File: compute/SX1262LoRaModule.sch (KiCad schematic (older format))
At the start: 28 parts, among them U201 SX1262, U202 PE4259, Y201 TBD

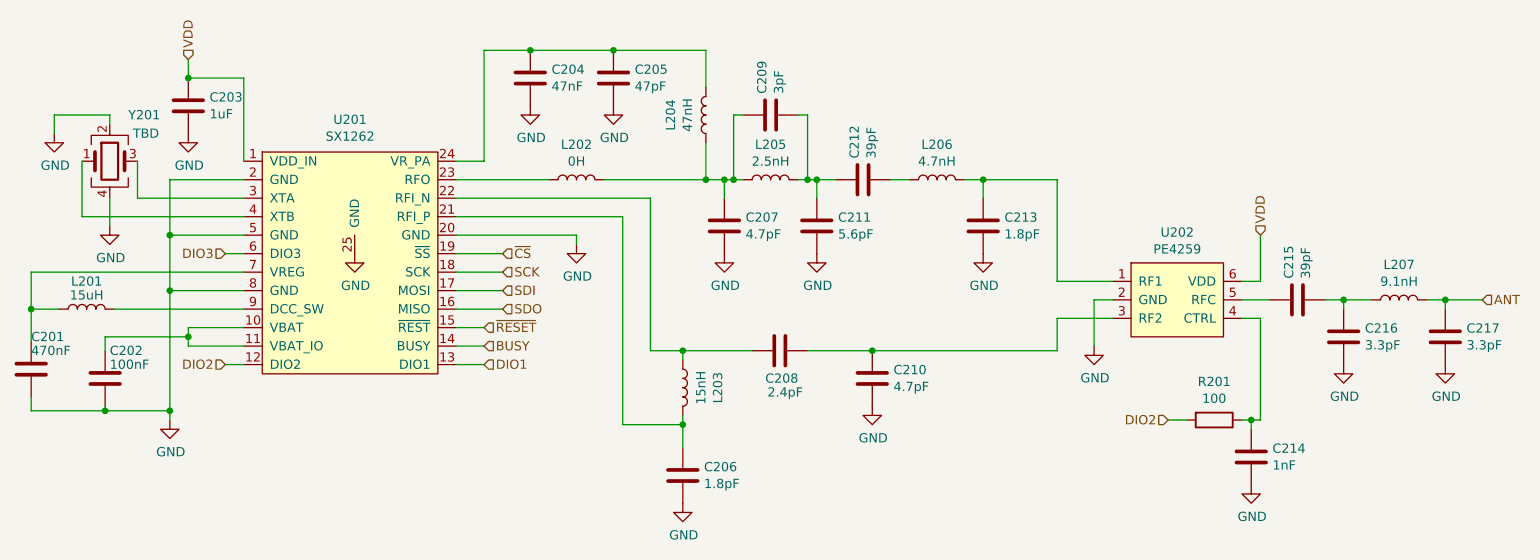
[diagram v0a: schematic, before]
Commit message: Adding more GND testpoints
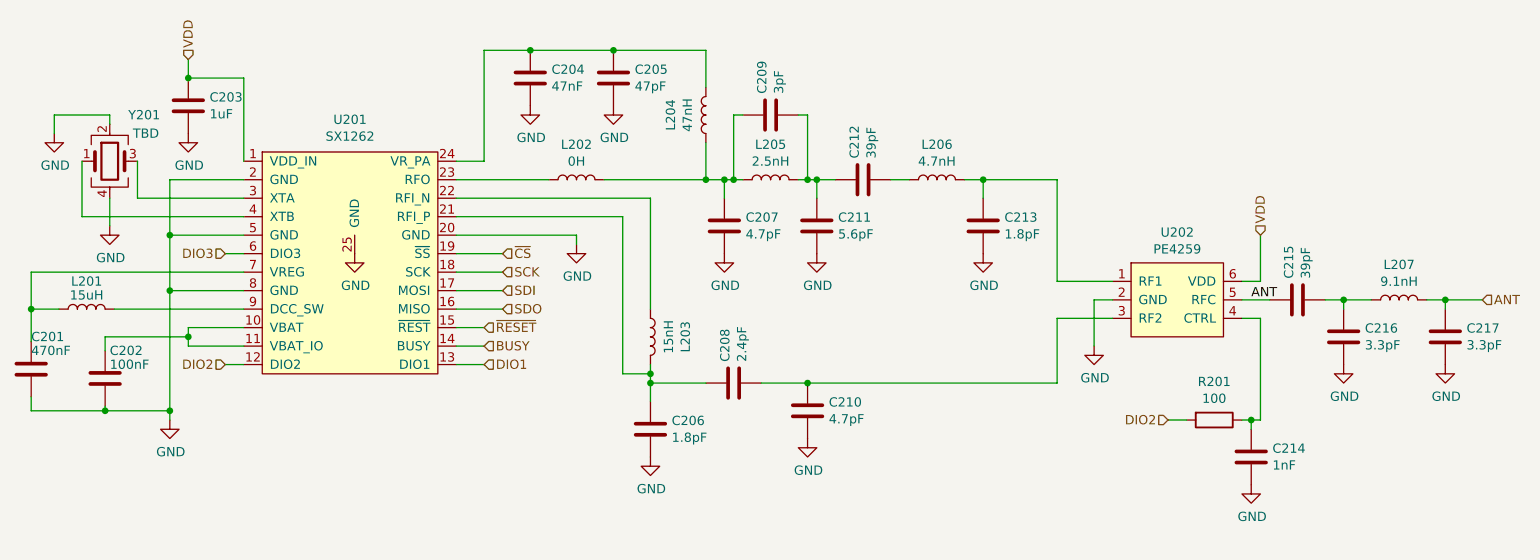
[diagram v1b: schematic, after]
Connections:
- net ANT: now also C215.1, U202.5 (RFC)
- net at L203.1, U201.22 (RFI_N): no longer C208.1
- net at C206.1, L203.2, U201.21 (RFI_P): now also C208.1
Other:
- moved on the sheet: C206, C208, C210, L203
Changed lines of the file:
@@
 L Device:L L203
 U 1 1 618C8BAD
-P 6025 4425
+P 5850 4150
 AR Path="/624C3AFD/618C8BAD" Ref="L203"  Part="1"
 AR Path="/61FFC2A4/618C8BAD" Ref="L?"  Part="1"
-F 0 "L203" V 6215 4425 50  0000 C CNN
-F 1 "15nH" V 6124 4425 50  0000 C CNN
-F 2 "Inductor_SMD:L_0402_1005Metric_Pad0.77x0.64mm_HandSolder" H 6025 4425 50  0001 C CNN
-F 3 "~" H 6025 4425 50  0001 C CNN
-F 4 "" V 6025 4425 50  0001 C CNN "MFN"
-F 5 "" V 6025 4425 50  0001 C CNN "MFP"
-F 6 "" V 6025 4425 50  0001 C CNN "S1PN"
-F 7 "" V 6025 4425 50  0001 C CNN "S1PL"
-F 8 "DNL" V 6025 4425 50  0001 C CNN "Notes"
-	1    6025 4425
+F 0 "L203" V 6040 4150 50  0000 C CNN
+F 1 "15nH" V 5949 4150 50  0000 C CNN
+F 2 "Inductor_SMD:L_0402_1005Metric_Pad0.77x0.64mm_HandSolder" H 5850 4150 50  0001 C CNN
+F 3 "~" H 5850 4150 50  0001 C CNN
+F 4 "" V 5850 4150 50  0001 C CNN "MFN"
+F 5 "" V 5850 4150 50  0001 C CNN "MFP"
+F 6 "" V 5850 4150 50  0001 C CNN "S1PN"
+F 7 "" V 5850 4150 50  0001 C CNN "S1PL"
+F 8 "DNL" V 5850 4150 50  0001 C CNN "Notes"
+	1    5850 4150
 	1    0    0    -1
 $EndComp
 Wire Wire Line
 	4800 3400 5850 3400
+Wire Wire Line
+	5850 3400 5850 4000
 Wire Wire Line
 	4800 3500 5700 3500
@@
 L Device:C C206
 U 1 1 618CE91A
-P 6025 4900
+P 5850 4650
 AR Path="/624C3AFD/618CE91A" Ref="C206"  Part="1"
 AR Path="/61FFC2A4/618CE91A" Ref="C?"  Part="1"
-F 0 "C206" H 6140 4946 50  0000 L CNN
-F 1 "1.8pF" H 6140 4855 50  0000 L CNN
-F 2 "Capacitor_SMD:C_0402_1005Metric_Pad0.74x0.62mm_HandSolder" H 6063 4750 50  0001 C CNN
-F 3 "~" H 6025 4900 50  0001 C CNN
-F 4 "" H 6025 4900 50  0001 C CNN "MFN"
-F 5 "" H 6025 4900 50  0001 C CNN "MFP"
-F 6 "" H 6025 4900 50  0001 C CNN "S1PN"
-F 7 "" H 6025 4900 50  0001 C CNN "S1PL"
-F 8 "DNL" H 6025 4900 50  0001 C CNN "Notes"
-	1    6025 4900
-	1    0    0    -1
-$EndComp
+F 0 "C206" H 5965 4696 50  0000 L CNN
+F 1 "1.8pF" H 5965 4605 50  0000 L CNN
+F 2 "Capacitor_SMD:C_0402_1005Metric_Pad0.74x0.62mm_HandSolder" H 5888 4500 50  0001 C CNN
+F 3 "~" H 5850 4650 50  0001 C CNN
+F 4 "" H 5850 4650 50  0001 C CNN "MFN"
+F 5 "" H 5850 4650 50  0001 C CNN "MFP"
+F 6 "" H 5850 4650 50  0001 C CNN "S1PN"
+F 7 "" H 5850 4650 50  0001 C CNN "S1PL"
+F 8 "DNL" H 5850 4650 50  0001 C CNN "Notes"
+	1    5850 4650
+	1    0    0    -1
+$EndComp
+Wire Wire Line
+	5850 4300 5850 4350
+Wire Wire Line
+	5700 4350 5850 4350
+Wire Wire Line
+	5700 3500 5700 4350
+Connection ~ 5850 4350
 $Comp
 L power:GND #PWR0209
 U 1 1 618D373E
-P 6025 5050
+P 5850 4800
 AR Path="/624C3AFD/618D373E" Ref="#PWR0209"  Part="1"
 AR Path="/61FFC2A4/618D373E" Ref="#PWR?"  Part="1"
-F 0 "#PWR0209" H 6025 4800 50  0001 C CNN
-F 1 "GND" H 6030 4877 50  0000 C CNN
-F 2 "" H 6025 5050 50  0001 C CNN
-F 3 "" H 6025 5050 50  0001 C CNN
-	1    6025 5050
+F 0 "#PWR0209" H 5850 4550 50  0001 C CNN
+F 1 "GND" H 5855 4627 50  0000 C CNN
+F 2 "" H 5850 4800 50  0001 C CNN
+F 3 "" H 5850 4800 50  0001 C CNN
+	1    5850 4800
 	1    0    0    -1
 $EndComp
@@
 L Device:C C208
 U 1 1 618D3CBD
-P 6550 4225
+P 6300 4400
 AR Path="/624C3AFD/618D3CBD" Ref="C208"  Part="1"
 AR Path="/61FFC2A4/618D3CBD" Ref="C?"  Part="1"
-F 0 "C208" V 6400 4125 50  0000 L CNN
-F 1 "2.4pF" V 6325 4100 50  0000 L CNN
-F 2 "Capacitor_SMD:C_0402_1005Metric_Pad0.74x0.62mm_HandSolder" H 6588 4075 50  0001 C CNN
-F 3 "~" H 6550 4225 50  0001 C CNN
-F 4 "" H 6550 4225 50  0001 C CNN "MFN"
-F 5 "" H 6550 4225 50  0001 C CNN "MFP"
-F 6 "Digikey" H 6550 4225 50  0001 C CNN "S1PN"
-F 7 "https://www.digikey.com/en/products/detail/taiyo-yuden/EVK105CH0R3BW-F/1169601" H 6550 4225 50  0001 C CNN "S1PL"
-F 8 "DNL" H 6550 4225 50  0001 C CNN "Notes"
-	1    6550 4225
+F 0 "C208" H 6415 4446 50  0000 L CNN
+F 1 "2.4pF" H 6415 4355 50  0000 L CNN
+F 2 "Capacitor_SMD:C_0402_1005Metric_Pad0.74x0.62mm_HandSolder" H 6338 4250 50  0001 C CNN
+F 3 "~" H 6300 4400 50  0001 C CNN
+F 4 "" H 6300 4400 50  0001 C CNN "MFN"
+F 5 "" H 6300 4400 50  0001 C CNN "MFP"
+F 6 "Digikey" H 6300 4400 50  0001 C CNN "S1PN"
+F 7 "https://www.digikey.com/en/products/detail/taiyo-yuden/EVK105CH0R3BW-F/1169601" H 6300 4400 50  0001 C CNN "S1PL"
+F 8 "DNL" H 6300 4400 50  0001 C CNN "Notes"
+	1    6300 4400
 	0    -1   -1   0
 $EndComp
@@
 L Device:C C210
 U 1 1 618D4647
-P 7050 4375
+P 6700 4550
 AR Path="/624C3AFD/618D4647" Ref="C210"  Part="1"
 AR Path="/61FFC2A4/618D4647" Ref="C?"  Part="1"
-F 0 "C210" H 7165 4421 50  0000 L CNN
-F 1 "4.7pF" H 7165 4330 50  0000 L CNN
-F 2 "Capacitor_SMD:C_0402_1005Metric_Pad0.74x0.62mm_HandSolder" H 7088 4225 50  0001 C CNN
-F 3 "~" H 7050 4375 50  0001 C CNN
-F 4 "" H 7050 4375 50  0001 C CNN "MFN"
-F 5 "" H 7050 4375 50  0001 C CNN "MFP"
-F 6 "" H 7050 4375 50  0001 C CNN "S1PN"
-F 7 "" H 7050 4375 50  0001 C CNN "S1PL"
-F 8 "DNL" H 7050 4375 50  0001 C CNN "Notes"
-	1    7050 4375
-	1    0    0    -1
-$EndComp
+F 0 "C210" H 6815 4596 50  0000 L CNN
+F 1 "4.7pF" H 6815 4505 50  0000 L CNN
+F 2 "Capacitor_SMD:C_0402_1005Metric_Pad0.74x0.62mm_HandSolder" H 6738 4400 50  0001 C CNN
+F 3 "~" H 6700 4550 50  0001 C CNN
+F 4 "" H 6700 4550 50  0001 C CNN "MFN"
+F 5 "" H 6700 4550 50  0001 C CNN "MFP"
+F 6 "" H 6700 4550 50  0001 C CNN "S1PN"
+F 7 "" H 6700 4550 50  0001 C CNN "S1PL"
+F 8 "DNL" H 6700 4550 50  0001 C CNN "Notes"
+	1    6700 4550
+	1    0    0    -1
+$EndComp
+Wire Wire Line
+	5850 4350 5850 4400
+Wire Wire Line
+	5850 4400 6150 4400
+Connection ~ 5850 4400
+Wire Wire Line
+	5850 4400 5850 4500
+Wire Wire Line
+	6450 4400 6700 4400
 $Comp
 L power:GND #PWR0211
 U 1 1 618DD2D6
-P 7050 4525
+P 6700 4700
 AR Path="/624C3AFD/618DD2D6" Ref="#PWR0211"  Part="1"
 AR Path="/61FFC2A4/618DD2D6" Ref="#PWR?"  Part="1"
-F 0 "#PWR0211" H 7050 4275 50  0001 C CNN
-F 1 "GND" H 7055 4352 50  0000 C CNN
-F 2 "" H 7050 4525 50  0001 C CNN
-F 3 "" H 7050 4525 50  0001 C CNN
-	1    7050 4525
-	1    0    0    -1
-$EndComp
+F 0 "#PWR0211" H 6700 4450 50  0001 C CNN
+F 1 "GND" H 6705 4527 50  0000 C CNN
+F 2 "" H 6700 4700 50  0001 C CNN
+F 3 "" H 6700 4700 50  0001 C CNN
+	1    6700 4700
+	1    0    0    -1
+$EndComp
+Wire Wire Line
+	6700 4400 8050 4400
+Connection ~ 6700 4400
 Wire Wire Line
 	8050 3300 8050 3850
 Wire Wire Line
 	8050 3850 8350 3850
+Wire Wire Line
+	8050 4400 8050 4050
 Wire Wire Line
 	8350 4050 8050 4050
@@
 	1    0    0    -1
 $EndComp
+Text Label 9100 3950 0    50   ~ 0
+ANT
 $Comp
 L Device:L L201
@@
 Wire Wire Line
 	3650 3400 3075 3400
-Wire Wire Line
-	6700 4225 7050 4225
-Wire Wire Line
-	8050 4225 8050 4050
-Connection ~ 7050 4225
-Wire Wire Line
-	7050 4225 8050 4225
-Wire Wire Line
-	5850 3400 5850 4225
-Wire Wire Line
-	5850 4225 6025 4225
-Connection ~ 6025 4225
-Wire Wire Line
-	6025 4225 6400 4225
-Wire Wire Line
-	6025 4225 6025 4275
-Wire Wire Line
-	5700 3500 5700 4625
-Wire Wire Line
-	6025 4625 6025 4750
-Wire Wire Line
-	6025 4625 6025 4575
-Connection ~ 6025 4625
-Wire Wire Line
-	5700 4625 6025 4625
 $EndSCHEMATC

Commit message: Revert "Adding more GND testpoints"
This reverts commit 458bd6481f51bde2da150f265f3cf5d6fabf7a4a.
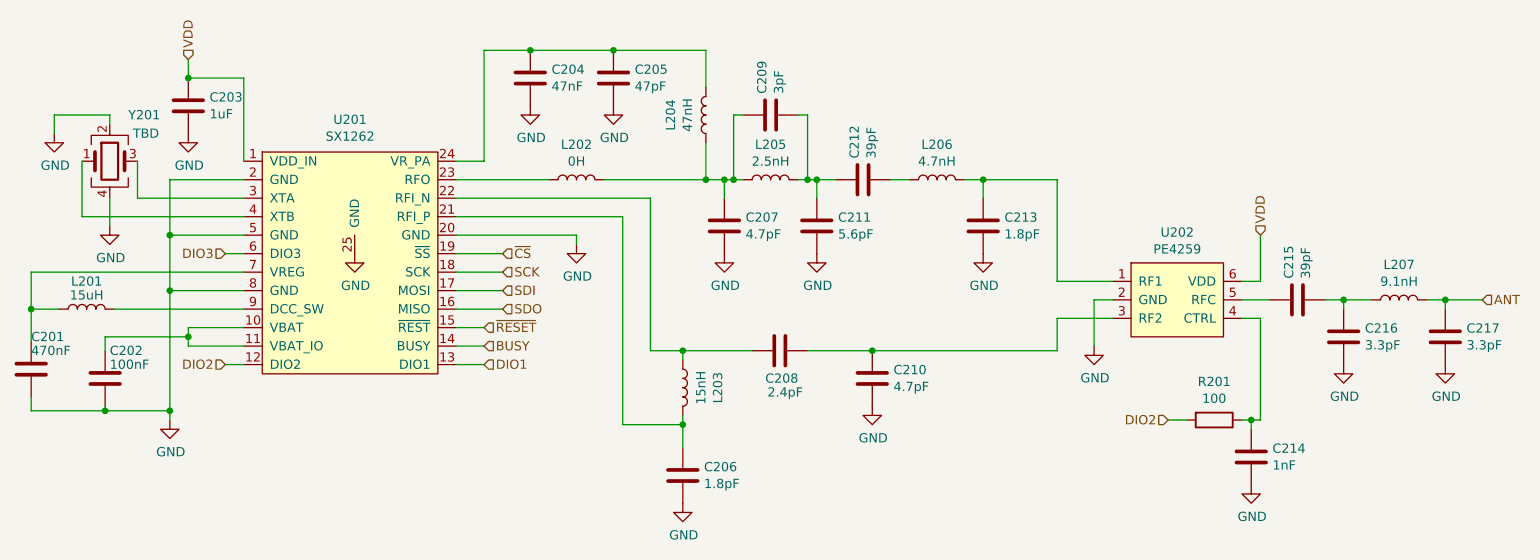
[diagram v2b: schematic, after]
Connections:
- net ANT: no longer C215.1, U202.5 (RFC)
- net at L203.1, U201.22 (RFI_N): now also C208.1
- net at C206.1, L203.2, U201.21 (RFI_P): no longer C208.1
- new net: C215.1, U202.5 (RFC)
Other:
- moved on the sheet: C206, C208, C210, L203
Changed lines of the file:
@@
 L Device:L L203
 U 1 1 618C8BAD
-P 5850 4150
+P 6025 4425
 AR Path="/624C3AFD/618C8BAD" Ref="L203"  Part="1"
 AR Path="/61FFC2A4/618C8BAD" Ref="L?"  Part="1"
-F 0 "L203" V 6040 4150 50  0000 C CNN
-F 1 "15nH" V 5949 4150 50  0000 C CNN
-F 2 "Inductor_SMD:L_0402_1005Metric_Pad0.77x0.64mm_HandSolder" H 5850 4150 50  0001 C CNN
-F 3 "~" H 5850 4150 50  0001 C CNN
-F 4 "" V 5850 4150 50  0001 C CNN "MFN"
-F 5 "" V 5850 4150 50  0001 C CNN "MFP"
-F 6 "" V 5850 4150 50  0001 C CNN "S1PN"
-F 7 "" V 5850 4150 50  0001 C CNN "S1PL"
-F 8 "DNL" V 5850 4150 50  0001 C CNN "Notes"
-	1    5850 4150
+F 0 "L203" V 6215 4425 50  0000 C CNN
+F 1 "15nH" V 6124 4425 50  0000 C CNN
+F 2 "Inductor_SMD:L_0402_1005Metric_Pad0.77x0.64mm_HandSolder" H 6025 4425 50  0001 C CNN
+F 3 "~" H 6025 4425 50  0001 C CNN
+F 4 "" V 6025 4425 50  0001 C CNN "MFN"
+F 5 "" V 6025 4425 50  0001 C CNN "MFP"
+F 6 "" V 6025 4425 50  0001 C CNN "S1PN"
+F 7 "" V 6025 4425 50  0001 C CNN "S1PL"
+F 8 "DNL" V 6025 4425 50  0001 C CNN "Notes"
+	1    6025 4425
 	1    0    0    -1
 $EndComp
 Wire Wire Line
 	4800 3400 5850 3400
-Wire Wire Line
-	5850 3400 5850 4000
 Wire Wire Line
 	4800 3500 5700 3500
@@
 L Device:C C206
 U 1 1 618CE91A
-P 5850 4650
+P 6025 4900
 AR Path="/624C3AFD/618CE91A" Ref="C206"  Part="1"
 AR Path="/61FFC2A4/618CE91A" Ref="C?"  Part="1"
-F 0 "C206" H 5965 4696 50  0000 L CNN
-F 1 "1.8pF" H 5965 4605 50  0000 L CNN
-F 2 "Capacitor_SMD:C_0402_1005Metric_Pad0.74x0.62mm_HandSolder" H 5888 4500 50  0001 C CNN
-F 3 "~" H 5850 4650 50  0001 C CNN
-F 4 "" H 5850 4650 50  0001 C CNN "MFN"
-F 5 "" H 5850 4650 50  0001 C CNN "MFP"
-F 6 "" H 5850 4650 50  0001 C CNN "S1PN"
-F 7 "" H 5850 4650 50  0001 C CNN "S1PL"
-F 8 "DNL" H 5850 4650 50  0001 C CNN "Notes"
-	1    5850 4650
-	1    0    0    -1
-$EndComp
-Wire Wire Line
-	5850 4300 5850 4350
-Wire Wire Line
-	5700 4350 5850 4350
-Wire Wire Line
-	5700 3500 5700 4350
-Connection ~ 5850 4350
+F 0 "C206" H 6140 4946 50  0000 L CNN
+F 1 "1.8pF" H 6140 4855 50  0000 L CNN
+F 2 "Capacitor_SMD:C_0402_1005Metric_Pad0.74x0.62mm_HandSolder" H 6063 4750 50  0001 C CNN
+F 3 "~" H 6025 4900 50  0001 C CNN
+F 4 "" H 6025 4900 50  0001 C CNN "MFN"
+F 5 "" H 6025 4900 50  0001 C CNN "MFP"
+F 6 "" H 6025 4900 50  0001 C CNN "S1PN"
+F 7 "" H 6025 4900 50  0001 C CNN "S1PL"
+F 8 "DNL" H 6025 4900 50  0001 C CNN "Notes"
+	1    6025 4900
+	1    0    0    -1
+$EndComp
 $Comp
 L power:GND #PWR0209
 U 1 1 618D373E
-P 5850 4800
+P 6025 5050
 AR Path="/624C3AFD/618D373E" Ref="#PWR0209"  Part="1"
 AR Path="/61FFC2A4/618D373E" Ref="#PWR?"  Part="1"
-F 0 "#PWR0209" H 5850 4550 50  0001 C CNN
-F 1 "GND" H 5855 4627 50  0000 C CNN
-F 2 "" H 5850 4800 50  0001 C CNN
-F 3 "" H 5850 4800 50  0001 C CNN
-	1    5850 4800
+F 0 "#PWR0209" H 6025 4800 50  0001 C CNN
+F 1 "GND" H 6030 4877 50  0000 C CNN
+F 2 "" H 6025 5050 50  0001 C CNN
+F 3 "" H 6025 5050 50  0001 C CNN
+	1    6025 5050
 	1    0    0    -1
 $EndComp
@@
 L Device:C C208
 U 1 1 618D3CBD
-P 6300 4400
+P 6550 4225
 AR Path="/624C3AFD/618D3CBD" Ref="C208"  Part="1"
 AR Path="/61FFC2A4/618D3CBD" Ref="C?"  Part="1"
-F 0 "C208" H 6415 4446 50  0000 L CNN
-F 1 "2.4pF" H 6415 4355 50  0000 L CNN
-F 2 "Capacitor_SMD:C_0402_1005Metric_Pad0.74x0.62mm_HandSolder" H 6338 4250 50  0001 C CNN
-F 3 "~" H 6300 4400 50  0001 C CNN
-F 4 "" H 6300 4400 50  0001 C CNN "MFN"
-F 5 "" H 6300 4400 50  0001 C CNN "MFP"
-F 6 "Digikey" H 6300 4400 50  0001 C CNN "S1PN"
-F 7 "https://www.digikey.com/en/products/detail/taiyo-yuden/EVK105CH0R3BW-F/1169601" H 6300 4400 50  0001 C CNN "S1PL"
-F 8 "DNL" H 6300 4400 50  0001 C CNN "Notes"
-	1    6300 4400
+F 0 "C208" V 6400 4125 50  0000 L CNN
+F 1 "2.4pF" V 6325 4100 50  0000 L CNN
+F 2 "Capacitor_SMD:C_0402_1005Metric_Pad0.74x0.62mm_HandSolder" H 6588 4075 50  0001 C CNN
+F 3 "~" H 6550 4225 50  0001 C CNN
+F 4 "" H 6550 4225 50  0001 C CNN "MFN"
+F 5 "" H 6550 4225 50  0001 C CNN "MFP"
+F 6 "Digikey" H 6550 4225 50  0001 C CNN "S1PN"
+F 7 "https://www.digikey.com/en/products/detail/taiyo-yuden/EVK105CH0R3BW-F/1169601" H 6550 4225 50  0001 C CNN "S1PL"
+F 8 "DNL" H 6550 4225 50  0001 C CNN "Notes"
+	1    6550 4225
 	0    -1   -1   0
 $EndComp
@@
 L Device:C C210
 U 1 1 618D4647
-P 6700 4550
+P 7050 4375
 AR Path="/624C3AFD/618D4647" Ref="C210"  Part="1"
 AR Path="/61FFC2A4/618D4647" Ref="C?"  Part="1"
-F 0 "C210" H 6815 4596 50  0000 L CNN
-F 1 "4.7pF" H 6815 4505 50  0000 L CNN
-F 2 "Capacitor_SMD:C_0402_1005Metric_Pad0.74x0.62mm_HandSolder" H 6738 4400 50  0001 C CNN
-F 3 "~" H 6700 4550 50  0001 C CNN
-F 4 "" H 6700 4550 50  0001 C CNN "MFN"
-F 5 "" H 6700 4550 50  0001 C CNN "MFP"
-F 6 "" H 6700 4550 50  0001 C CNN "S1PN"
-F 7 "" H 6700 4550 50  0001 C CNN "S1PL"
-F 8 "DNL" H 6700 4550 50  0001 C CNN "Notes"
-	1    6700 4550
-	1    0    0    -1
-$EndComp
-Wire Wire Line
-	5850 4350 5850 4400
-Wire Wire Line
-	5850 4400 6150 4400
-Connection ~ 5850 4400
-Wire Wire Line
-	5850 4400 5850 4500
-Wire Wire Line
-	6450 4400 6700 4400
+F 0 "C210" H 7165 4421 50  0000 L CNN
+F 1 "4.7pF" H 7165 4330 50  0000 L CNN
+F 2 "Capacitor_SMD:C_0402_1005Metric_Pad0.74x0.62mm_HandSolder" H 7088 4225 50  0001 C CNN
+F 3 "~" H 7050 4375 50  0001 C CNN
+F 4 "" H 7050 4375 50  0001 C CNN "MFN"
+F 5 "" H 7050 4375 50  0001 C CNN "MFP"
+F 6 "" H 7050 4375 50  0001 C CNN "S1PN"
+F 7 "" H 7050 4375 50  0001 C CNN "S1PL"
+F 8 "DNL" H 7050 4375 50  0001 C CNN "Notes"
+	1    7050 4375
+	1    0    0    -1
+$EndComp
 $Comp
 L power:GND #PWR0211
 U 1 1 618DD2D6
-P 6700 4700
+P 7050 4525
 AR Path="/624C3AFD/618DD2D6" Ref="#PWR0211"  Part="1"
 AR Path="/61FFC2A4/618DD2D6" Ref="#PWR?"  Part="1"
-F 0 "#PWR0211" H 6700 4450 50  0001 C CNN
-F 1 "GND" H 6705 4527 50  0000 C CNN
-F 2 "" H 6700 4700 50  0001 C CNN
-F 3 "" H 6700 4700 50  0001 C CNN
-	1    6700 4700
-	1    0    0    -1
-$EndComp
-Wire Wire Line
-	6700 4400 8050 4400
-Connection ~ 6700 4400
+F 0 "#PWR0211" H 7050 4275 50  0001 C CNN
+F 1 "GND" H 7055 4352 50  0000 C CNN
+F 2 "" H 7050 4525 50  0001 C CNN
+F 3 "" H 7050 4525 50  0001 C CNN
+	1    7050 4525
+	1    0    0    -1
+$EndComp
 Wire Wire Line
 	8050 3300 8050 3850
 Wire Wire Line
 	8050 3850 8350 3850
-Wire Wire Line
-	8050 4400 8050 4050
 Wire Wire Line
 	8350 4050 8050 4050
@@
 	1    0    0    -1
 $EndComp
-Text Label 9100 3950 0    50   ~ 0
-ANT
 $Comp
 L Device:L L201
@@
 Wire Wire Line
 	3650 3400 3075 3400
+Wire Wire Line
+	6700 4225 7050 4225
+Wire Wire Line
+	8050 4225 8050 4050
+Connection ~ 7050 4225
+Wire Wire Line
+	7050 4225 8050 4225
+Wire Wire Line
+	5850 3400 5850 4225
+Wire Wire Line
+	5850 4225 6025 4225
+Connection ~ 6025 4225
+Wire Wire Line
+	6025 4225 6400 4225
+Wire Wire Line
+	6025 4225 6025 4275
+Wire Wire Line
+	5700 3500 5700 4625
+Wire Wire Line
+	6025 4625 6025 4750
+Wire Wire Line
+	6025 4625 6025 4575
+Connection ~ 6025 4625
+Wire Wire Line
+	5700 4625 6025 4625
 $EndSCHEMATC
